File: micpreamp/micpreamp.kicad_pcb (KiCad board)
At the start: 2 copper layers, 73.7 x 34.3 mm, 17 parts, among them J1 Input, J2 Output, J3 Vdd, J4 Gnd, U1 3.3 reg, U2 LM358

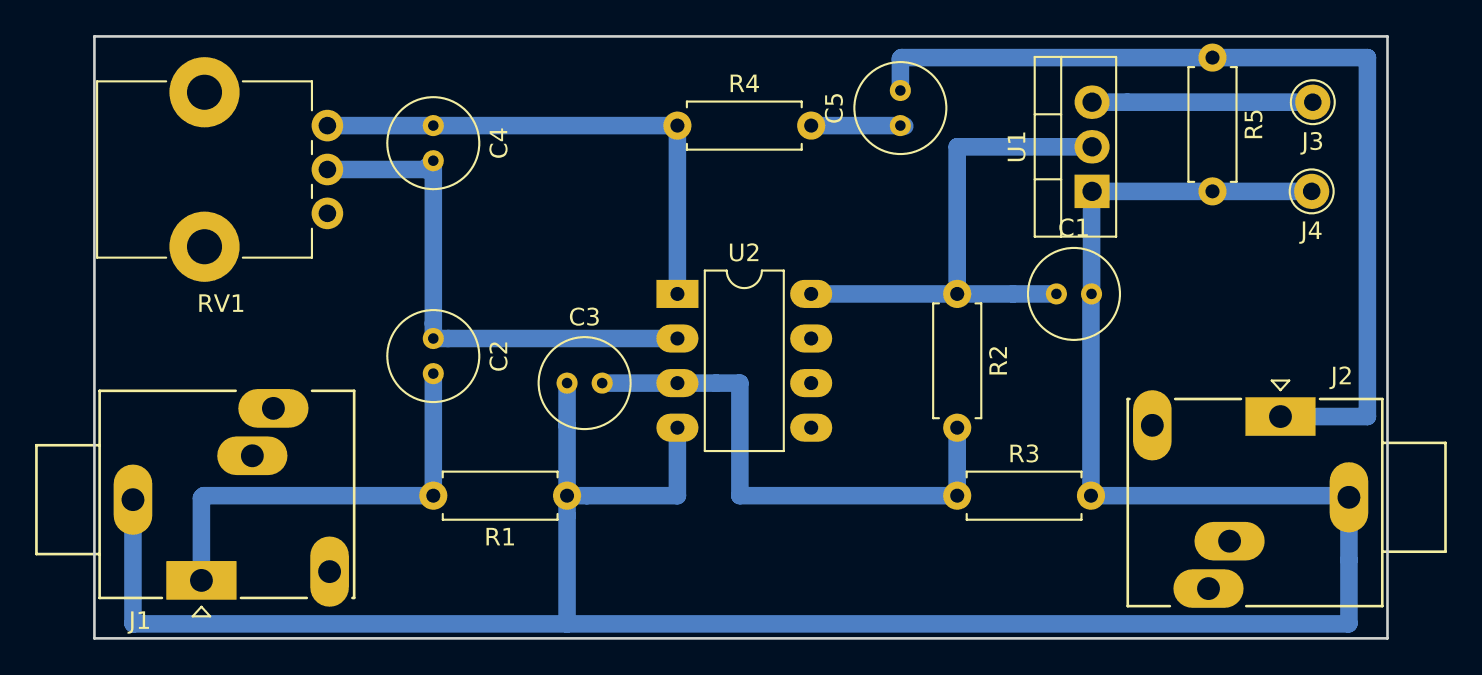
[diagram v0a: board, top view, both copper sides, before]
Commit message: added tiny spi proj and fixed an error with the mic preamp
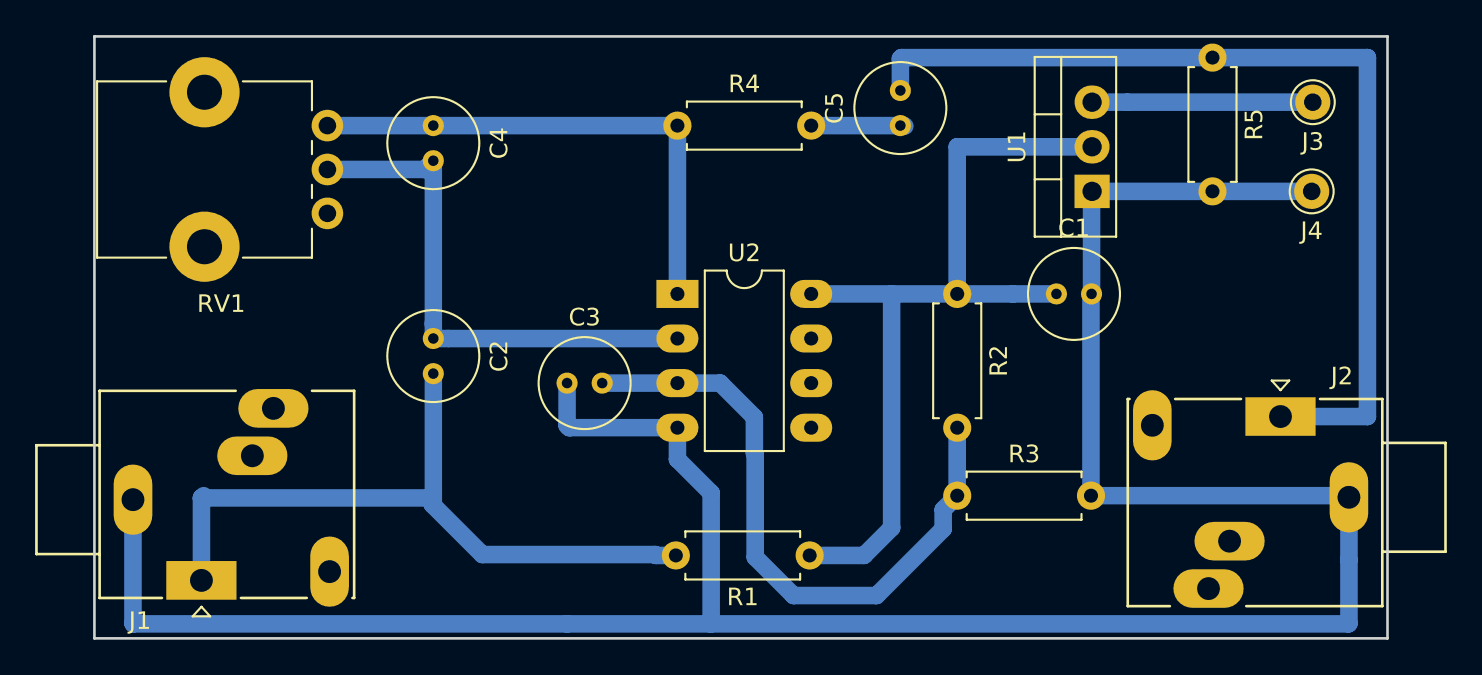
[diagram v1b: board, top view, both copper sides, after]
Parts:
- moved R1 14.2 mm to (91.5, 147.7)
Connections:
- R1 pad 1: GND -> Net-(C1-Pad1)
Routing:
- net Net-(C1-Pad1): track 30.0 -> 48.7 mm
- net Net-(C2-Pad2): track 24.9 -> 40.7 mm
- net Net-(C3-Pad2): track 30.5 -> 36.8 mm
- net GND: track 152.0 -> 148.9 mm
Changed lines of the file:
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@@
     (thickness 1.6)
     (drawings 10)
-    (tracks 56)
+    (tracks 74)
     (zones 0)
     (modules 17)
@@
   )
   (module Resistor_THT:R_Axial_DIN0207_L6.3mm_D2.5mm_P7.62mm_Horizontal (layer F.Cu)
-    (at 77.724 144.272 180)
+    (at 91.5416 147.6756 180)
     (descr "Resistor, Axial_DIN0207 series, Axial, Horizontal, pin pitch=7.62mm, 0.25W = 1/4W, length*diameter=6.3*2.5mm^2, http://cdn-reichelt.de/documents/datenblatt/B400/1_4W%23YAG.pdf")
     (tags "Resistor Axial_DIN0207 series Axial Horizontal pin pitch 7.62mm 0.25W = 1/4W length 6.3mm diameter 2.5mm")
@@
       (net 3 "Net-(C2-Pad2)"))
     (pad 1 thru_hole circle (at 0 0 180) (size 1.6 1.6) (drill 0.8) (layers *.Cu *.Mask)
-      (net 2 GND))
+      (net 1 "Net-(C1-Pad1)"))
     (model ${KISYS3DMOD}/Resistor_THT.3dshapes/R_Axial_DIN0207_L6.3mm_D2.5mm_P7.62mm_Horizontal.wrl
       (at (xyz 0 0 0))
@@
     (arrow2b (pts (xy 50.8 166.37) (xy 51.926504 165.783579)))
   )
-  (segment (start 91.6305 132.7785) (end 99.949 132.7785) (width 1) (layer B.Cu) (net 1))
   (segment (start 105.6005 132.7785) (end 103.124 132.7785) (width 1) (layer B.Cu) (net 1))
   (segment (start 99.949 132.7785) (end 103.124 132.7785) (width 1) (layer B.Cu) (net 1))
   (segment (start 99.949 124.3965) (end 99.949 132.7785) (width 1) (layer B.Cu) (net 1))
   (segment (start 107.6325 124.3965) (end 99.949 124.3965) (width 1) (layer B.Cu) (net 1))
-  (segment (start 77.724 145.40337) (end 77.724 151.5745) (width 1) (layer B.Cu) (net 2))
-  (segment (start 77.724 144.272) (end 77.724 145.40337) (width 1) (layer B.Cu) (net 2))
-  (segment (start 77.724 144.272) (end 77.724 140.2715) (width 1) (layer B.Cu) (net 2))
+  (segment (start 96.2152 146.1008) (end 96.2152 132.7785) (width 1) (layer B.Cu) (net 1))
+  (segment (start 94.6404 147.6756) (end 96.2152 146.1008) (width 1) (layer B.Cu) (net 1))
+  (segment (start 91.5416 147.6756) (end 94.6404 147.6756) (width 1) (layer B.Cu) (net 1))
+  (segment (start 91.6305 132.7785) (end 96.2152 132.7785) (width 1) (layer B.Cu) (net 1))
+  (segment (start 96.2152 132.7785) (end 99.949 132.7785) (width 1) (layer B.Cu) (net 1))
   (segment (start 77.724 140.2715) (end 77.724 137.8585) (width 1) (layer B.Cu) (net 2))
   (segment (start 122.1725 144.272) (end 122.264 144.3635) (width 1) (layer B.Cu) (net 2))
@@
   (segment (start 107.6325 126.9365) (end 114.4905 126.9365) (width 1) (layer B.Cu) (net 2))
   (segment (start 114.4905 126.9365) (end 120.142 126.9365) (width 1) (layer B.Cu) (net 2))
-  (segment (start 84.0105 140.3985) (end 84.0105 144.272) (width 1) (layer B.Cu) (net 2))
-  (segment (start 78.85537 144.272) (end 77.724 144.272) (width 1) (layer B.Cu) (net 2))
-  (segment (start 84.0105 144.272) (end 78.85537 144.272) (width 1) (layer B.Cu) (net 2))
   (segment (start 122.264 151.548) (end 122.264 147.9285) (width 1) (layer B.Cu) (net 2))
   (segment (start 122.264 147.9285) (end 122.264 144.3635) (width 1) (layer B.Cu) (net 2))
-  (segment (start 77.724 151.5745) (end 122.2375 151.5745) (width 1) (layer B.Cu) (net 2))
   (segment (start 122.2375 151.5745) (end 122.264 151.548) (width 1) (layer B.Cu) (net 2))
   (segment (start 52.996 151.548) (end 52.996 144.498) (width 1) (layer B.Cu) (net 2))
   (segment (start 77.724 151.5745) (end 53.0225 151.5745) (width 1) (layer B.Cu) (net 2))
   (segment (start 53.0225 151.5745) (end 52.996 151.548) (width 1) (layer B.Cu) (net 2))
-  (segment (start 57.023 144.272) (end 70.104 144.272) (width 1) (layer B.Cu) (net 3))
+  (segment (start 84.0105 142.1985) (end 85.9316 144.1196) (width 1) (layer B.Cu) (net 2))
+  (segment (start 84.0105 140.3985) (end 84.0105 142.1985) (width 1) (layer B.Cu) (net 2))
+  (segment (start 85.9316 151.5457) (end 85.9028 151.5745) (width 1) (layer B.Cu) (net 2))
+  (segment (start 85.9316 144.1196) (end 85.9316 151.5457) (width 1) (layer B.Cu) (net 2))
+  (segment (start 77.724 151.5745) (end 85.9028 151.5745) (width 1) (layer B.Cu) (net 2))
+  (segment (start 85.9028 151.5745) (end 122.2375 151.5745) (width 1) (layer B.Cu) (net 2))
+  (segment (start 77.851 140.3985) (end 77.724 140.2715) (width 1) (layer B.Cu) (net 2))
+  (segment (start 84.0105 140.3985) (end 77.851 140.3985) (width 1) (layer B.Cu) (net 2))
   (segment (start 56.896 149.098) (end 56.896 144.399) (width 1) (layer B.Cu) (net 3))
   (segment (start 56.896 144.399) (end 57.023 144.272) (width 1) (layer B.Cu) (net 3))
-  (segment (start 70.104 144.272) (end 70.104 137.3185) (width 1) (layer B.Cu) (net 3))
+  (segment (start 82.79023 147.6756) (end 82.73943 147.6248) (width 1) (layer B.Cu) (net 3))
+  (segment (start 83.9216 147.6756) (end 82.79023 147.6756) (width 1) (layer B.Cu) (net 3))
+  (segment (start 82.73943 147.6248) (end 72.898 147.6248) (width 1) (layer B.Cu) (net 3))
+  (segment (start 72.898 147.6248) (end 70.0532 144.78) (width 1) (layer B.Cu) (net 3))
+  (segment (start 70.0532 144.78) (end 70.104 144.7292) (width 1) (layer B.Cu) (net 3))
+  (segment (start 69.8754 144.399) (end 70.104 144.1704) (width 1) (layer B.Cu) (net 3))
+  (segment (start 56.896 144.399) (end 69.8754 144.399) (width 1) (layer B.Cu) (net 3))
+  (segment (start 70.104 144.7292) (end 70.104 144.1704) (width 1) (layer B.Cu) (net 3))
+  (segment (start 70.104 144.1704) (end 70.104 137.3185) (width 1) (layer B.Cu) (net 3))
   (segment (start 69.604 125.69) (end 70.104 125.19) (width 1) (layer B.Cu) (net 4))
   (segment (start 64.0715 125.69) (end 69.604 125.69) (width 1) (layer B.Cu) (net 4))
@@
   (segment (start 79.724 137.8585) (end 84.0105 137.8585) (width 1) (layer B.Cu) (net 5))
   (segment (start 99.949 140.3985) (end 99.949 144.272) (width 1) (layer B.Cu) (net 5))
-  (segment (start 86.2105 137.8585) (end 84.0105 137.8585) (width 1) (layer B.Cu) (net 5))
-  (segment (start 87.5665 137.8585) (end 86.2105 137.8585) (width 1) (layer B.Cu) (net 5))
-  (segment (start 99.949 144.272) (end 87.5665 144.272) (width 1) (layer B.Cu) (net 5))
-  (segment (start 87.5665 144.272) (end 87.5665 137.8585) (width 1) (layer B.Cu) (net 5))
+  (segment (start 99.149001 145.071999) (end 99.149001 146.164199) (width 1) (layer B.Cu) (net 5))
+  (segment (start 99.949 144.272) (end 99.149001 145.071999) (width 1) (layer B.Cu) (net 5))
+  (segment (start 99.149001 146.164199) (end 95.3516 149.9616) (width 1) (layer B.Cu) (net 5))
+  (segment (start 95.3516 149.9616) (end 90.6272 149.9616) (width 1) (layer B.Cu) (net 5))
+  (segment (start 90.6272 149.9616) (end 88.4428 147.7772) (width 1) (layer B.Cu) (net 5))
+  (segment (start 88.4428 141.8908) (end 88.392 141.84) (width 1) (layer B.Cu) (net 5))
+  (segment (start 88.4428 147.7772) (end 88.4428 141.8908) (width 1) (layer B.Cu) (net 5))
+  (segment (start 88.392 141.84) (end 88.392 139.8016) (width 1) (layer B.Cu) (net 5))
+  (segment (start 86.4489 137.8585) (end 84.0105 137.8585) (width 1) (layer B.Cu) (net 5))
+  (segment (start 88.392 139.8016) (end 86.4489 137.8585) (width 1) (layer B.Cu) (net 5))
   (segment (start 84.0105 132.7785) (end 84.0105 123.19) (width 1) (layer B.Cu) (net 6))
   (segment (start 84.0105 123.19) (end 70.104 123.19) (width 1) (layer B.Cu) (net 6))
